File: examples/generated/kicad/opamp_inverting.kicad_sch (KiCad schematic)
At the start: 7 parts

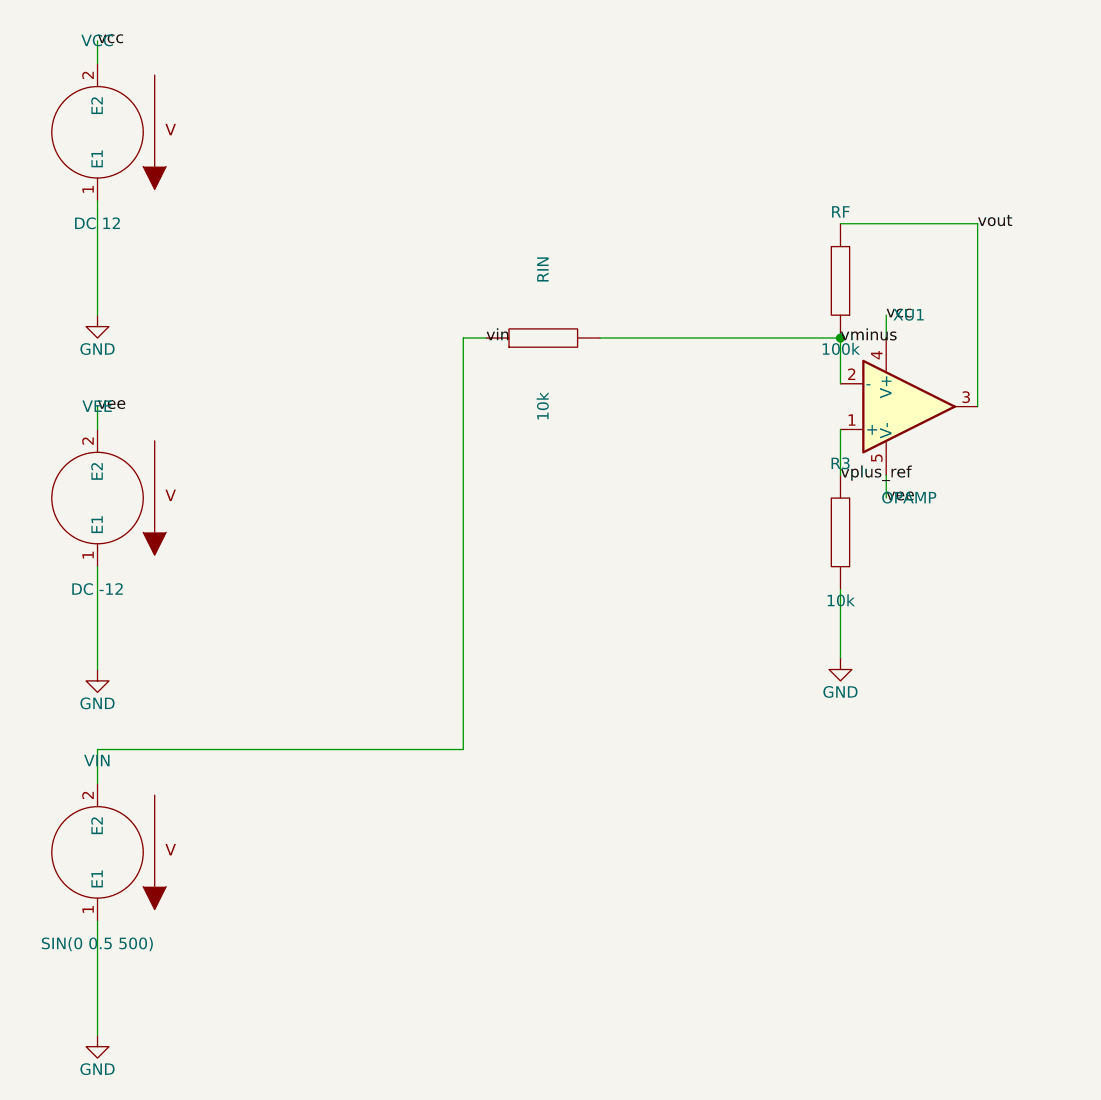
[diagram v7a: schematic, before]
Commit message: Attempt to fix non-inverting op-amp power net labels.
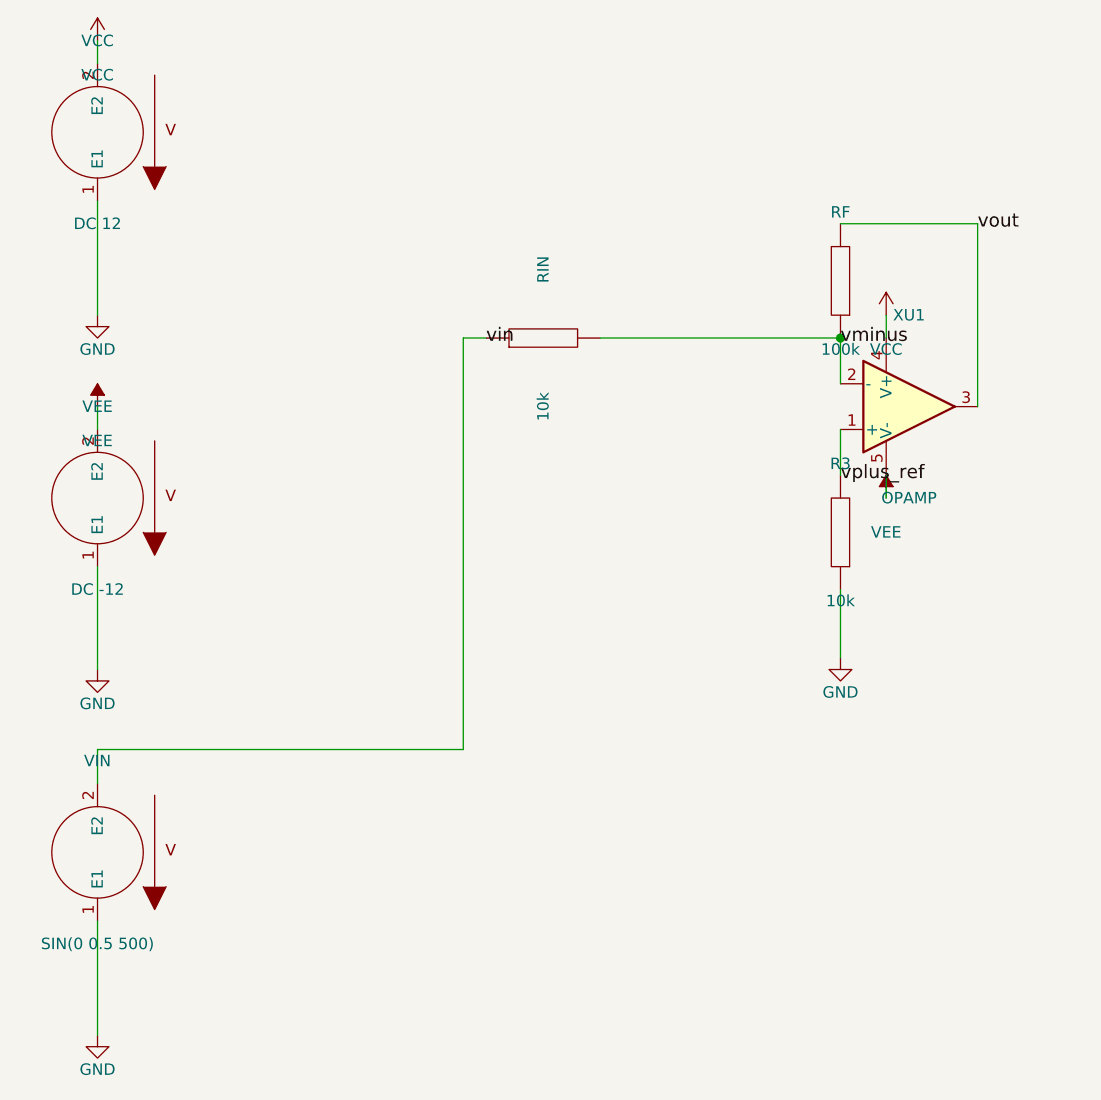
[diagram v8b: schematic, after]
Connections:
- net vcc renamed VCC
- net vee renamed VEE
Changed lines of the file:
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@@
+    )
+  )
+  (symbol (lib_id "VCC") (at 80.01 49.53 0) (unit 1)
+    (in_bom yes) (on_board yes)
+    (property "Reference" "#PWR0005" (at 80.01 45.72 0)
+      (effects (font (size 1.27 1.27)) hide)
+    )
+    (property "Value" "VCC" (at 80.01 53.34 0)
+      (effects (font (size 1.27 1.27)))
+    )
+    (property "Footprint" "" (at 0 0 0)
+      (effects (font (size 1.27 1.27)) hide)
+    )
+    (property "Datasheet" "" (at 0 0 0)
+      (effects (font (size 1.27 1.27)) hide)
+    )
+  )
+  (symbol (lib_id "VCC") (at 167.64 80.01 0) (unit 1)
+    (in_bom yes) (on_board yes)
+    (property "Reference" "#PWR0006" (at 167.64 76.2 0)
+      (effects (font (size 1.27 1.27)) hide)
+    )
+    (property "Value" "VCC" (at 167.64 83.82000000000001 0)
+      (effects (font (size 1.27 1.27)))
+    )
+    (property "Footprint" "" (at 0 0 0)
+      (effects (font (size 1.27 1.27)) hide)
+    )
+    (property "Datasheet" "" (at 0 0 0)
+      (effects (font (size 1.27 1.27)) hide)
+    )
+  )
+  (symbol (lib_id "VEE") (at 80.01 90.17 0) (unit 1)
+    (in_bom yes) (on_board yes)
+    (property "Reference" "#PWR0007" (at 80.01 86.36 0)
+      (effects (font (size 1.27 1.27)) hide)
+    )
+    (property "Value" "VEE" (at 80.01 93.98 0)
+      (effects (font (size 1.27 1.27)))
+    )
+    (property "Footprint" "" (at 0 0 0)
+      (effects (font (size 1.27 1.27)) hide)
+    )
+    (property "Datasheet" "" (at 0 0 0)
+      (effects (font (size 1.27 1.27)) hide)
+    )
+  )
+  (symbol (lib_id "VEE") (at 167.64 100.33 0) (unit 1)
+    (in_bom yes) (on_board yes)
+    (property "Reference" "#PWR0008" (at 167.64 96.52 0)
+      (effects (font (size 1.27 1.27)) hide)
+    )
+    (property "Value" "VEE" (at 167.64 104.14 0)
+      (effects (font (size 1.27 1.27)))
+    )
+    (property "Footprint" "" (at 0 0 0)
+      (effects (font (size 1.27 1.27)) hide)
+    )
+    (property "Datasheet" "" (at 0 0 0)
+      (effects (font (size 1.27 1.27)) hide)
     )
   )
@@
     )
   )
-  (label "vcc" (at 167.64 80.01 0)
-    (effects (font (size 1.27 1.27)))
-  )
-  (label "vcc" (at 80.01 49.53 0)
-    (effects (font (size 1.27 1.27)))
-  )
-  (label "vee" (at 167.64 100.33 0)
-    (effects (font (size 1.27 1.27)))
-  )
-  (label "vee" (at 80.01 90.17 0)
-    (effects (font (size 1.27 1.27)))
-  )
   (label "vin" (at 123.19 82.55 0)
-    (effects (font (size 1.27 1.27)))
+    (effects (font (size 1.50 1.50)))
   )
   (label "vplus_ref" (at 162.56 97.79 0)
-    (effects (font (size 1.27 1.27)))
+    (effects (font (size 1.50 1.50)))
   )
   (label "vminus" (at 162.56 82.55 0)
-    (effects (font (size 1.27 1.27)))
+    (effects (font (size 1.50 1.50)))
   )
   (label "vout" (at 177.80 69.85 0)
-    (effects (font (size 1.27 1.27)))
+    (effects (font (size 1.50 1.50)))
+  )
+  (wire (pts (xy 80.01 67.31) (xy 80.01 80.01))
+    (stroke (width 0) (type solid) (color 0 0 0 0))
+  )
+  (wire (pts (xy 80.01 107.95) (xy 80.01 119.38))
+    (stroke (width 0) (type solid) (color 0 0 0 0))
+  )
+  (wire (pts (xy 80.01 147.32) (xy 80.01 160.02))
+    (stroke (width 0) (type solid) (color 0 0 0 0))
+  )
+  (wire (pts (xy 80.01 132.08) (xy 80.01 128.27))
+    (stroke (width 0) (type solid) (color 0 0 0 0))
+  )
+  (wire (pts (xy 80.01 128.27) (xy 120.65 128.27))
+    (stroke (width 0) (type solid) (color 0 0 0 0))
+  )
+  (wire (pts (xy 120.65 128.27) (xy 120.65 82.55))
+    (stroke (width 0) (type solid) (color 0 0 0 0))
+  )
+  (wire (pts (xy 120.65 82.55) (xy 123.19 82.55))
+    (stroke (width 0) (type solid) (color 0 0 0 0))
+  )
+  (wire (pts (xy 162.56 92.71) (xy 162.56 97.79))
+    (stroke (width 0) (type solid) (color 0 0 0 0))
+  )
+  (wire (pts (xy 162.56 110.49) (xy 162.56 118.11))
+    (stroke (width 0) (type solid) (color 0 0 0 0))
+  )
+  (wire (pts (xy 135.89 82.55) (xy 162.56 82.55))
+    (stroke (width 0) (type solid) (color 0 0 0 0))
+  )
+  (wire (pts (xy 162.56 87.63) (xy 162.56 82.55))
+    (stroke (width 0) (type solid) (color 0 0 0 0))
+  )
+  (wire (pts (xy 177.80 90.17) (xy 177.80 69.85))
+    (stroke (width 0) (type solid) (color 0 0 0 0))
+  )
+  (wire (pts (xy 162.56 69.85) (xy 177.80 69.85))
+    (stroke (width 0) (type solid) (color 0 0 0 0))
   )
   (wire (pts (xy 167.64 82.55) (xy 167.64 80.01))
@@
   )
   (wire (pts (xy 80.01 92.71) (xy 80.01 90.17))
-    (stroke (width 0) (type solid) (color 0 0 0 0))
-  )
-  (wire (pts (xy 80.01 67.31) (xy 80.01 80.01))
-    (stroke (width 0) (type solid) (color 0 0 0 0))
-  )
-  (wire (pts (xy 80.01 107.95) (xy 80.01 119.38))
-    (stroke (width 0) (type solid) (color 0 0 0 0))
-  )
-  (wire (pts (xy 80.01 147.32) (xy 80.01 160.02))
-    (stroke (width 0) (type solid) (color 0 0 0 0))
-  )
-  (wire (pts (xy 80.01 132.08) (xy 80.01 128.27))
-    (stroke (width 0) (type solid) (color 0 0 0 0))
-  )
-  (wire (pts (xy 80.01 128.27) (xy 120.65 128.27))
-    (stroke (width 0) (type solid) (color 0 0 0 0))
-  )
-  (wire (pts (xy 120.65 128.27) (xy 120.65 82.55))
-    (stroke (width 0) (type solid) (color 0 0 0 0))
-  )
-  (wire (pts (xy 120.65 82.55) (xy 123.19 82.55))
-    (stroke (width 0) (type solid) (color 0 0 0 0))
-  )
-  (wire (pts (xy 162.56 92.71) (xy 162.56 97.79))
-    (stroke (width 0) (type solid) (color 0 0 0 0))
-  )
-  (wire (pts (xy 162.56 110.49) (xy 162.56 118.11))
-    (stroke (width 0) (type solid) (color 0 0 0 0))
-  )
-  (wire (pts (xy 135.89 82.55) (xy 162.56 82.55))
-    (stroke (width 0) (type solid) (color 0 0 0 0))
-  )
-  (wire (pts (xy 162.56 87.63) (xy 162.56 82.55))
-    (stroke (width 0) (type solid) (color 0 0 0 0))
-  )
-  (wire (pts (xy 177.80 90.17) (xy 177.80 69.85))
-    (stroke (width 0) (type solid) (color 0 0 0 0))
-  )
-  (wire (pts (xy 162.56 69.85) (xy 177.80 69.85))
     (stroke (width 0) (type solid) (color 0 0 0 0))
   )
@@
     (path "/7d3a8dce-1385-5145-b651-aed84918d285" (reference "R3") (unit 1) (value "10k") (footprint ""))
     (path "/2cab4477-b53a-5241-99f6-3f0d34b69ae3" (reference "#PWR0001") (unit 1) (value "GND") (footprint ""))
+    (path "/e1c8a11a-69ea-5ef2-bfef-47b13bd91581" (reference "#PWR0005") (unit 1) (value "VCC") (footprint ""))
+    (path "/05a3b8a3-1d13-5fe2-9fae-7b9a999cfc11" (reference "#PWR0006") (unit 1) (value "VCC") (footprint ""))
+    (path "/e7b47471-234a-5d16-918d-6f7e270ded0c" (reference "#PWR0007") (unit 1) (value "VEE") (footprint ""))
+    (path "/fd98ea7a-d561-5af2-b677-b06c38871606" (reference "#PWR0008") (unit 1) (value "VEE") (footprint ""))
     (path "/09a203a8-be19-5256-bda7-017ceaed298c" (reference "VCC") (unit 1) (value "DC 12") (footprint ""))
     (path "/3c3e1f8b-94df-5470-936b-ecc90ba4b8cf" (reference "#PWR0002") (unit 1) (value "GND") (footprint ""))
